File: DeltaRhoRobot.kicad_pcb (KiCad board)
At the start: 4 copper layers, 70 x 75 mm, 120 parts, among them J1 Conn_01x02_Socket, J11 Conn_01x08, J13 Conn_02x09_Top_Bottom, J14 Conn_01x09, J15 Conn_02x09_Top_Bottom, J2 USB_C_Receptacle_USB2.0, J3 USB_C_Receptacle_USB2.0, J4 JST-XH, J5 JST-XH, J6 Conn_01x09, J7 Conn_02x20_Counter_Clockwise, J9 Conn_01x08, P1 B6B-ZRLFSN, P2 B6B-ZRLFSN, P3 B6B-ZRLFSN, P4 B6B-ZRLFSN, P5 B6B-ZRLFSN, P6 B6B-ZRLFSN, Q2 BSS138, Q5 BSS138, SW1 CAS-120A1, U10 ICM-42688-P, U11 LIS3MDL, U13 MIC5366-1.8YC5-TR, U14 W25Q16JVS, U2 AMS1117-3.3, U3 DRV8835DSSR, U4 RP2040, U5 DRV8835DSSR, U6 DRV8835DSSR, U7 TPS566242DRLR, U8 ESP32-S3-WROOM-1-N8R2, Y1 ABM8-272-T3

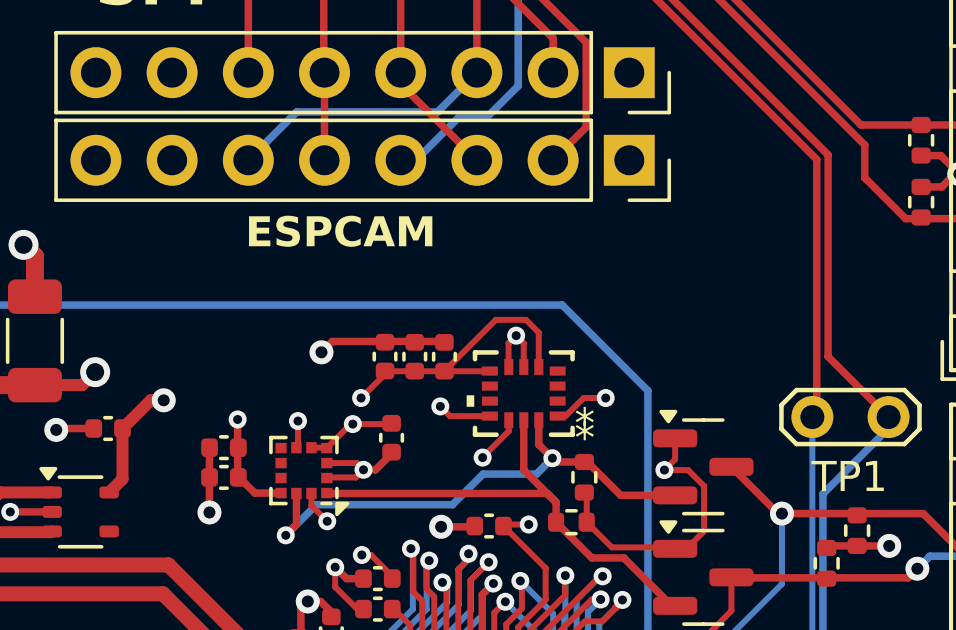
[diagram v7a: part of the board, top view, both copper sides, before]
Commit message: Silkscreen for orientation
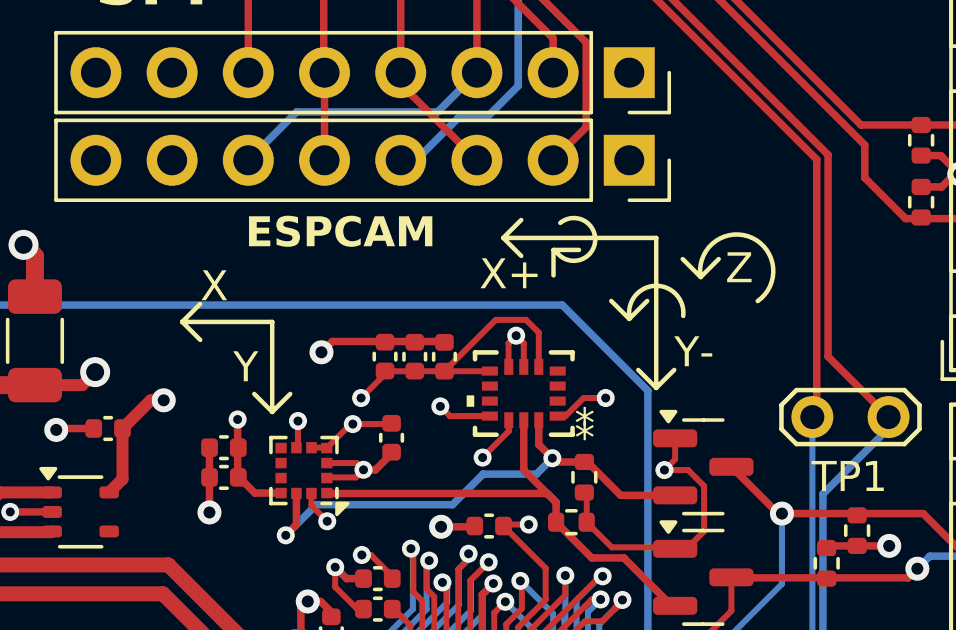
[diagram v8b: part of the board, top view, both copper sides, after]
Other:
- board text added: "X"
- board text added: "X+"
- board text added: "Y"
- board text added: "Y-"
- board text added: "Z"
